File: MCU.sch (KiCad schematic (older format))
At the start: 5 parts, among them J1 Conn_01x05, J2 Conn_01x09, U2 STM32F051K8Tx

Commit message: UPDATED SWITCH WIRING
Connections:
- net labels added: MCU_IMON
- net labels removed: MCU_ISENSE, SMBUS_INT
- wire segments 51 -> 50
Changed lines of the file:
@@
 	5250 2800 5775 2800
 Text HLabel 5775 2800 2    50   Input ~ 0
-MCU_ISENSE
+MCU_IMON
 Wire Wire Line
 	5250 2900 5775 2900
@@
 SMBUS_SMBA
 Wire Wire Line
-	4150 4000 3250 4000
-Text HLabel 3250 4000 0    50   Input ~ 0
-SMBUS_INT
-Wire Wire Line
 	5775 3600 5250 3600

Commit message: replaced stm32F051 with stm32F072
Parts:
- removed J2: Conn_01x09, symbol Connector_Generic:Conn_01x09
- removed U2: STM32F051K8Tx, Package_QFP:LQFP-32_7x7mm_P0.8mm, symbol MCU_ST_STM32F0:STM32F051K8Tx
- added C1, C2, C3, C4, C5, C6: 100nF, Capacitor_SMD:C_0805_2012Metric_Pad1.15x1.40mm_HandSolder, symbol Device:C
- added J2: Conn_01x14, symbol Connector_Generic:Conn_01x14
- added L1: BEAD, Inductor_SMD:L_0805_2012Metric_Pad1.15x1.40mm_HandSolder, symbol Device:L_Small
- added R4: 10K, Resistor_SMD:R_0805_2012Metric_Pad1.15x1.40mm_HandSolder, symbol Device:R
- added U2: STM32F072RBTx, Package_QFP:LQFP-64_10x10mm_P0.5mm, symbol MCU_ST_STM32F0:STM32F072RBTx
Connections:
- net labels added: AVDD, TFT_MISO, T_CLK, T_CS, T_DIN, T_IRQ, T_OUT
- wire segments 50 -> 101
- no-connect marks 10 -> 30
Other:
- note added: "ICP SOCKET"
- note added: "TOUCHSCREEN TFT LCD"
- note removed: "TFT_MISO"
- moved on the sheet: J1, R1, R2

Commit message: layout draft
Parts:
- J1: footprint (none) -> Connector_PinHeader_2.54mm:PinHeader_1x05_P2.54mm_Vertical
- J2: footprint (none) -> Connector_PinHeader_2.54mm:PinHeader_1x14_P2.54mm_Vertical
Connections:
- net MCU_SW: now reaches U2.16 (PA2)
- no-connect marks 30 -> 29
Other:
- moved on the sheet: C1, L1, R1, R2, R4, U2

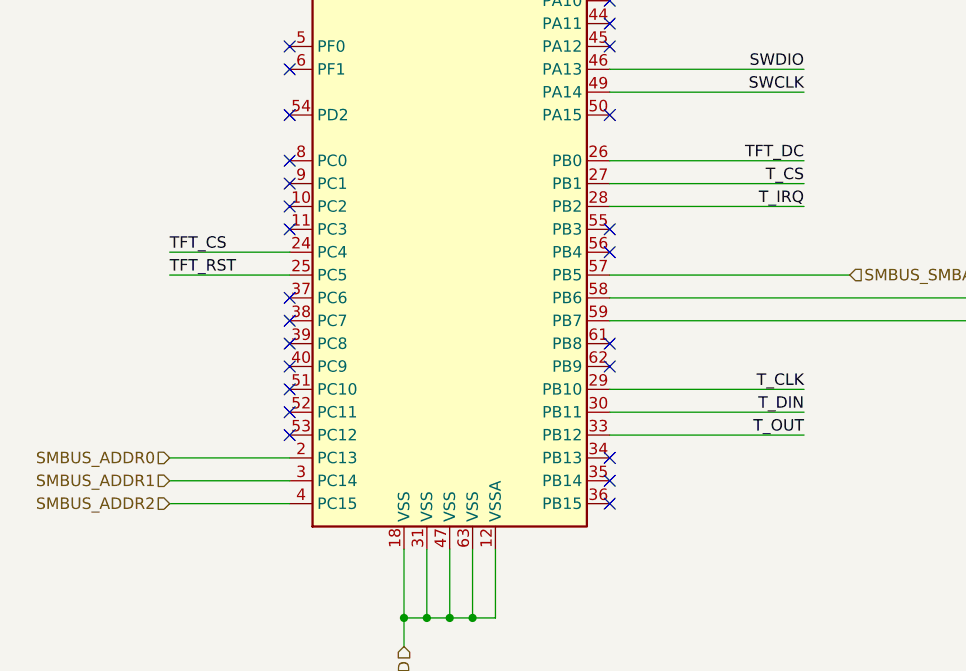
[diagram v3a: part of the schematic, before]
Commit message: moved SPI2 traces on MCU
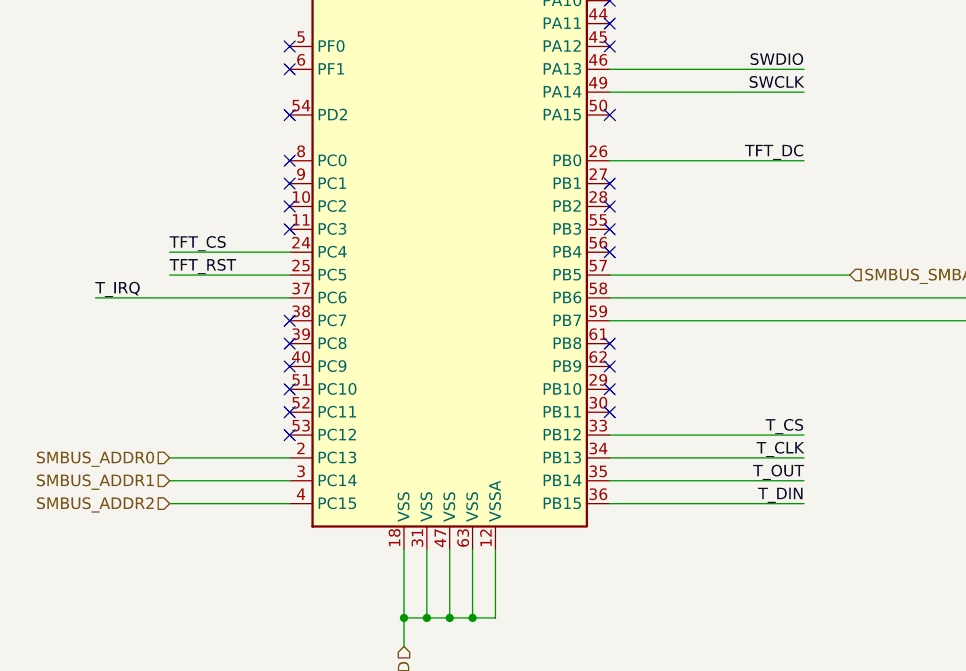
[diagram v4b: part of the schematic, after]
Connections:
- net T_CLK: now also U2.34 (PB13); no longer U2.29 (PB10)
- net T_CS: now also U2.33 (PB12); no longer U2.27 (PB1)
- net T_DIN: now also U2.36 (PB15); no longer U2.30 (PB11)
- net T_IRQ: now also U2.37 (PC6); no longer U2.28 (PB2)
- net T_OUT: now also U2.35 (PB14); no longer U2.33 (PB12)
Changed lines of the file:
@@
 TFT_MISO
 Wire Wire Line
-	4050 5350 4900 5350
-Wire Wire Line
-	4050 4450 4900 4450
-Wire Wire Line
-	4050 5450 4900 5450
+	4050 5650 4900 5650
 Wire Wire Line
 	4050 5550 4900 5550
 Wire Wire Line
-	4050 4550 4900 4550
-Text Label 4900 5350 2    50   ~ 0
+	4050 5850 4900 5850
+Wire Wire Line
+	4050 5750 4900 5750
+Wire Wire Line
+	2650 4950 1800 4950
+Text Label 4900 5650 2    50   ~ 0
 T_CLK
-Text Label 4900 4450 2    50   ~ 0
+Text Label 4900 5550 2    50   ~ 0
 T_CS
-Text Label 4900 5450 2    50   ~ 0
+Text Label 4900 5850 2    50   ~ 0
 T_DIN
-Text Label 4900 5550 2    50   ~ 0
+Text Label 4900 5750 2    50   ~ 0
 T_OUT
-Text Label 4900 4550 2    50   ~ 0
+Text Label 1800 4950 0    50   ~ 0
 T_IRQ
 NoConn ~ 4050 2950
@@
 NoConn ~ 4050 5150
 NoConn ~ 4050 5250
-NoConn ~ 4050 5650
-NoConn ~ 4050 5750
-NoConn ~ 4050 5850
 NoConn ~ 2650 5450
 NoConn ~ 2650 5350
@@
 NoConn ~ 2650 5150
 NoConn ~ 2650 5050
-NoConn ~ 2650 4950
+NoConn ~ 4050 4550
 NoConn ~ 2650 4650
 NoConn ~ 2650 4550
@@
 MCU_SW
 NoConn ~ 2650 5550
+NoConn ~ 4050 5350
+NoConn ~ 4050 5450
+NoConn ~ 4050 4450
 $EndSCHEMATC

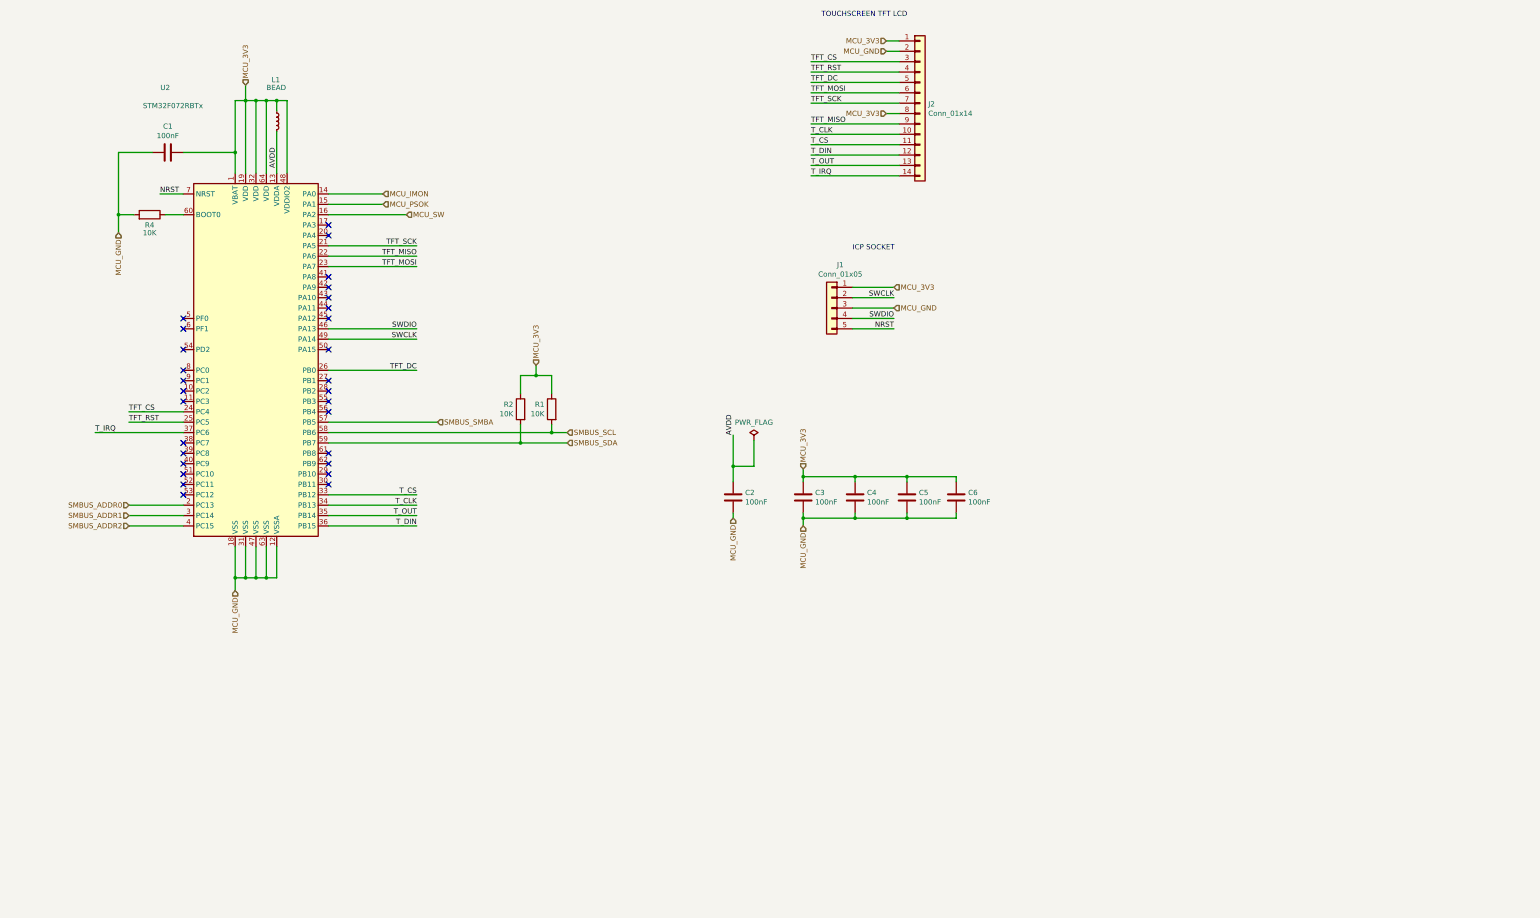
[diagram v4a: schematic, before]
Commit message: Added TFT Delayed Reset sub circuit
changed NCS1S1203SC to NCS1S1205SC
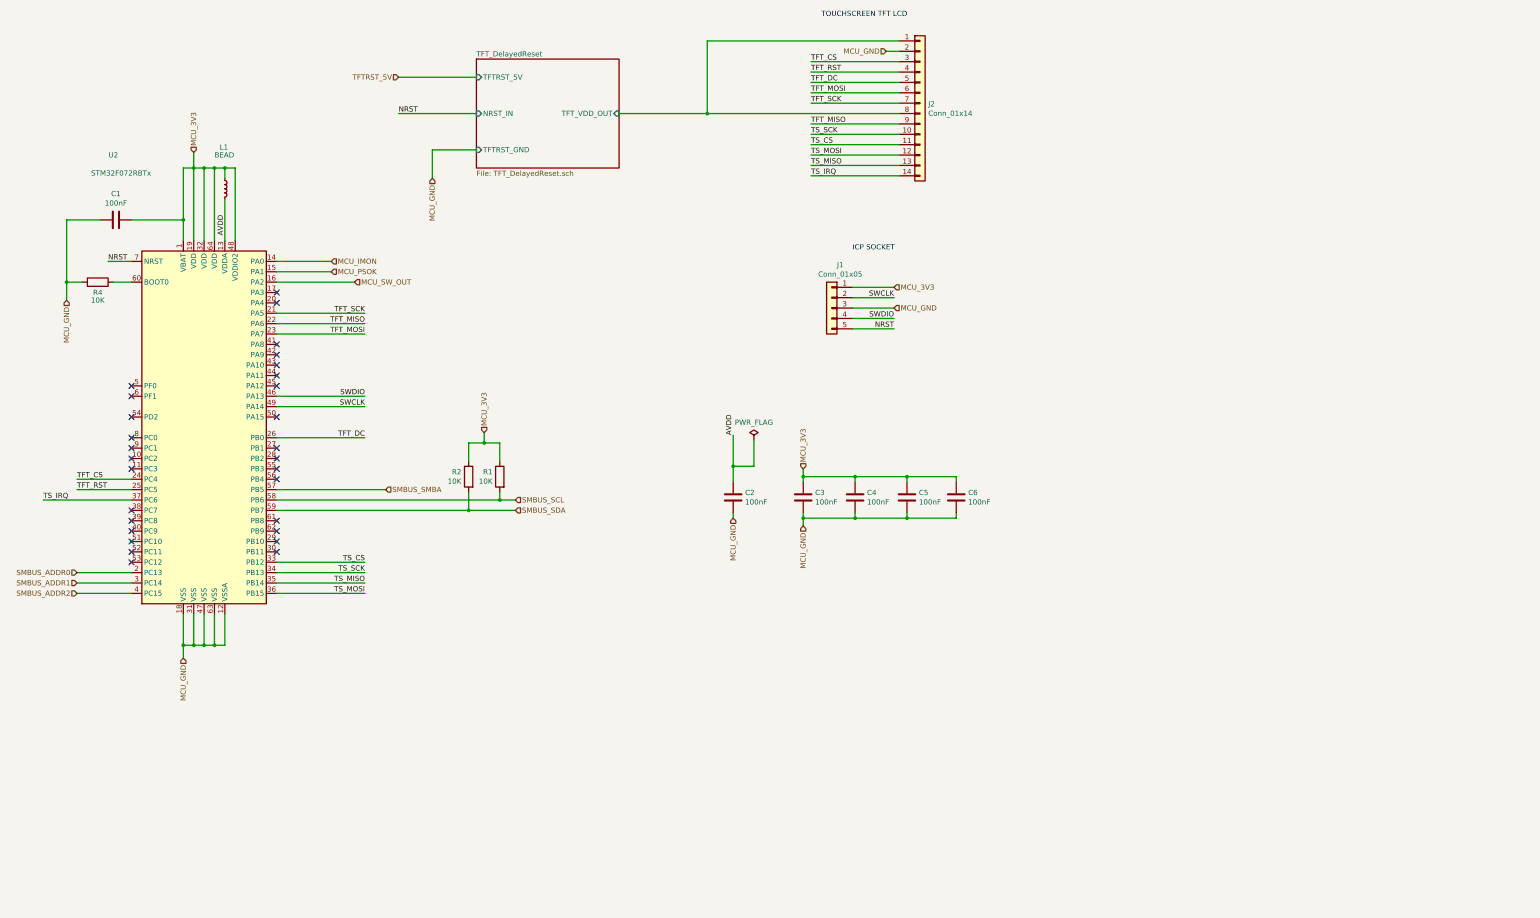
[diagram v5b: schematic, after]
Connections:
- net MCU_3V3: no longer J2.1 (Pin_1), J2.8 (Pin_8)
- net MCU_SW renamed MCU_SW_OUT
- net T_CLK renamed TS_SCK
- net T_CS renamed TS_CS
- net T_DIN renamed TS_MOSI
- net T_IRQ renamed TS_IRQ
- net T_OUT renamed TS_MISO
- new net TFT_DelayedReset/TFT_VDD_OUT: J2.1 (Pin_1), J2.8 (Pin_8)
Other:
- moved on the sheet: C1, L1, R1, R2, R4, U2

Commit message: updated hw
- added SMBUS address HW 
- Changed Isolated DC Module to TI SimpleSwitcher IC
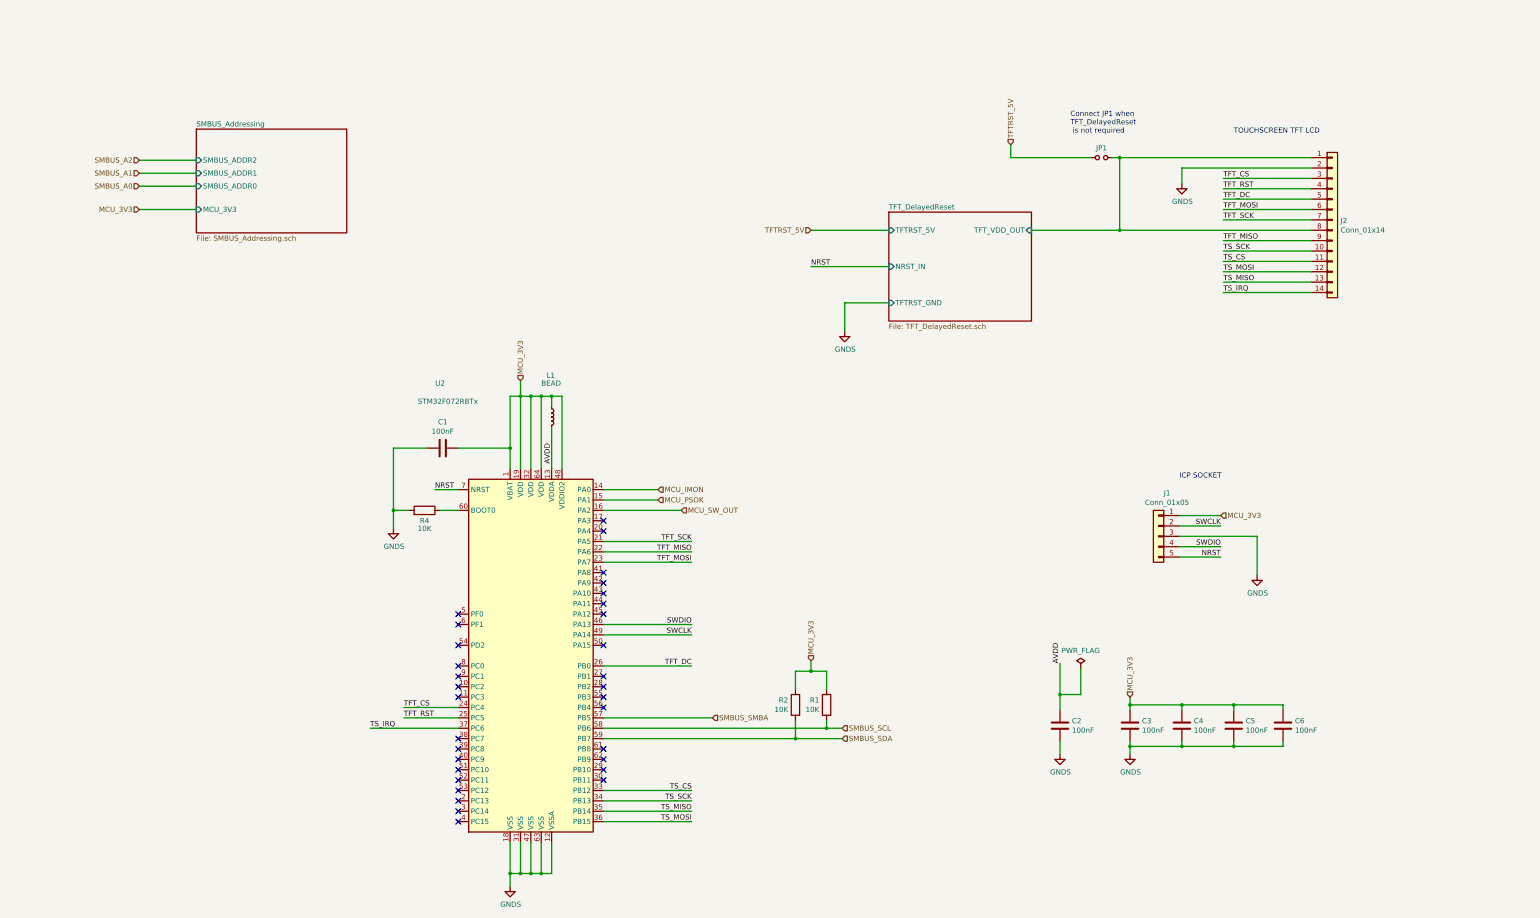
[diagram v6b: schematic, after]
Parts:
- added JP1: Jumper_NO_Small, Jumper:SolderJumper-2_P1.3mm_Open_Pad1.0x1.5mm, symbol Device:Jumper_NO_Small
- J1: footprint Connector_PinHeader_2.54mm:PinHeader_1x05_P2.54mm_Vertical -> Connector_PinHeader_2.54mm:PinHeader_1x05_P2.54mm_Horizontal
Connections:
- net TFTRST_5V: now also JP1.1
- net TFT_DelayedReset/TFT_VDD_OUT: now also JP1.2
- net MCU_GND renamed GNDS
- net SMBUS_ADDR0: no longer names the net of U2.2 (PC13)
- net SMBUS_ADDR1: no longer names the net of U2.3 (PC14)
- net SMBUS_ADDR2: no longer names the net of U2.4 (PC15)
- no-connect marks 29 -> 32
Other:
- note added: "Connect JP1 when\nTFT_DelayedReset\n is not required\n"
- moved on the sheet: C1, C2, C3, C4, C5, C6, J1, J2, L1, R1, R2, R4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

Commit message: Completed RevA
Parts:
- added TP1, TP2, TP? (x2): TestPoint, TestPoint:TestPoint_Pad_1.0x1.0mm, symbol Connector:TestPoint
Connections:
- net GNDS: now also TP2.1
- net MCU_3V3: now also TP1.1
- net SWCLK: now also TP?.1
- net SWDIO: now also TP?.1
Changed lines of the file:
@@
 $EndComp
 Wire Wire Line
-	12250 5750 12650 5750
+	12250 5750 13275 5750
 Wire Wire Line
 	12250 6050 12650 6050
@@
 Text Notes 12775 2075 0    50   ~ 0
 TOUCHSCREEN TFT LCD
-Text Notes 12250 5400 0    50   ~ 0
+Text Notes 11375 5975 0    50   ~ 0
 ICP SOCKET
 Wire Wire Line
@@
 NoConn ~ 6700 7300
 $Sheet
-S 9450 2825 1375 1050
+S 9450 2825 1375 700
 U 5F1755C4
 F0 "TFT_DelayedReset" 50
 F1 "TFT_DelayedReset.sch" 50
-F2 "TFTRST_GND" I L 9450 3700 50
 F3 "TFTRST_5V" I L 9450 3000 50
 F4 "TFT_VDD_OUT" I R 10825 3000 50
@@
 Wire Wire Line
 	11675 3000 13525 3000
-Wire Wire Line
-	9450 3700 9025 3700
-Wire Wire Line
-	9025 3700 9025 3975
 Text HLabel 11775 7500 1    50   Input ~ 0
 MCU_3V3
 Text HLabel 8700 7150 1    50   Input ~ 0
 MCU_3V3
-Text HLabel 12650 5750 2    50   Input ~ 0
+Text HLabel 13400 5750 2    50   Input ~ 0
 MCU_3V3
 Wire Wire Line
@@
 $EndComp
 Wire Wire Line
-	13000 5950 13000 6325
-Wire Wire Line
-	12250 5950 13000 5950
+	13825 5950 13825 6325
+Wire Wire Line
+	12250 5950 13825 5950
 $Comp
 L power:GNDS #PWR010
 U 1 1 5F506D40
-P 13000 6325
-F 0 "#PWR010" H 13000 6075 50  0001 C CNN
-F 1 "GNDS" H 13005 6152 50  0000 C CNN
-F 2 "" H 13000 6325 50  0001 C CNN
-F 3 "" H 13000 6325 50  0001 C CNN
-	1    13000 6325
+P 13825 6325
+F 0 "#PWR010" H 13825 6075 50  0001 C CNN
+F 1 "GNDS" H 13830 6152 50  0000 C CNN
+F 2 "" H 13825 6325 50  0001 C CNN
+F 3 "" H 13825 6325 50  0001 C CNN
+	1    13825 6325
 	1    0    0    -1
 $EndComp
@@
 Wire Wire Line
 	12275 2400 13525 2400
-$Comp
-L power:GNDS #PWR0103
-U 1 1 5F5B050D
-P 9025 3975
-F 0 "#PWR0103" H 9025 3725 50  0001 C CNN
-F 1 "GNDS" H 9030 3802 50  0000 C CNN
-F 2 "" H 9025 3975 50  0001 C CNN
-F 3 "" H 9025 3975 50  0001 C CNN
-	1    9025 3975
-	1    0    0    -1
-$EndComp
 Text Notes 11200 2075 0    50   ~ 0
 Connect JP1 when\nTFT_DelayedReset\n is not required\n
+$Comp
+L Connector:TestPoint TP1
+U 1 1 5F16AD63
+P 13275 5500
+F 0 "TP1" H 13333 5618 50  0000 L CNN
+F 1 "TestPoint" H 13333 5527 50  0000 L CNN
+F 2 "TestPoint:TestPoint_Pad_1.0x1.0mm" H 13475 5500 50  0001 C CNN
+F 3 "~" H 13475 5500 50  0001 C CNN
+	1    13275 5500
+	1    0    0    -1
+$EndComp
+Wire Wire Line
+	13275 5500 13275 5750
+Connection ~ 13275 5750
+Wire Wire Line
+	13275 5750 13400 5750
+$Comp
+L Connector:TestPoint TP2
+U 1 1 5F170479
+P 14025 5950
+F 0 "TP2" V 13950 6025 50  0000 L CNN
+F 1 "TestPoint" V 14125 6000 50  0000 L CNN
+F 2 "TestPoint:TestPoint_Pad_1.0x1.0mm" H 14225 5950 50  0001 C CNN
+F 3 "~" H 14225 5950 50  0001 C CNN
+	1    14025 5950
+	0    1    1    0
+$EndComp
+Wire Wire Line
+	14025 5950 13825 5950
+Connection ~ 13825 5950
+$Comp
+L Connector:TestPoint TP?
+U 1 1 5F271D97
+P 14650 5100
+AR Path="/5F02F4E9/5F271D97" Ref="TP?"  Part="1"
+AR Path="/5EFF0F4B/5F271D97" Ref="TP?"  Part="1"
+F 0 "TP?" H 14708 5218 50  0000 L CNN
+F 1 "TestPoint" H 14708 5127 50  0000 L CNN
+F 2 "TestPoint:TestPoint_Pad_1.0x1.0mm" H 14850 5100 50  0001 C CNN
+F 3 "~" H 14850 5100 50  0001 C CNN
+	1    14650 5100
+	1    0    0    -1
+$EndComp
+$Comp
+L Connector:TestPoint TP?
+U 1 1 5F275A4B
+P 15150 5100
+AR Path="/5F02F4E9/5F275A4B" Ref="TP?"  Part="1"
+AR Path="/5EFF0F4B/5F275A4B" Ref="TP?"  Part="1"
+F 0 "TP?" H 15208 5218 50  0000 L CNN
+F 1 "TestPoint" H 15208 5127 50  0000 L CNN
+F 2 "TestPoint:TestPoint_Pad_1.0x1.0mm" H 15350 5100 50  0001 C CNN
+F 3 "~" H 15350 5100 50  0001 C CNN
+	1    15150 5100
+	1    0    0    -1
+$EndComp
+Text Label 14650 5425 1    50   ~ 0
+SWCLK
+Wire Wire Line
+	14650 5100 14650 5425
+Text Label 15150 5425 1    50   ~ 0
+SWDIO
+Wire Wire Line
+	15150 5100 15150 5425
 $EndSCHEMATC

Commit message: save
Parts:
- J2: footprint Connector_PinHeader_2.54mm:PinHeader_1x14_P2.54mm_Vertical -> ILI9341_TFTLCD:ILI9341_ResitiveTouch_TFTLCD_2.8inch_85mm_50mm
- gave numbers to parts that had none: 2
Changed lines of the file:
@@
 F 0 "J2" H 13805 2892 50  0000 L CNN
 F 1 "Conn_01x14" H 13805 2801 50  0000 L CNN
-F 2 "Connector_PinHeader_2.54mm:PinHeader_1x14_P2.54mm_Vertical" H 13725 2900 50  0001 C CNN
+F 2 "ILI9341_TFTLCD:ILI9341_ResitiveTouch_TFTLCD_2.8inch_85mm_50mm" H 13725 2900 50  0001 C CNN
 F 3 "~" H 13725 2900 50  0001 C CNN
 	1    13725 2900
@@
 Connection ~ 13825 5950
 $Comp
-L Connector:TestPoint TP?
+L Connector:TestPoint TP22
 U 1 1 5F271D97
 P 14650 5100
-AR Path="/5F02F4E9/5F271D97" Ref="TP?"  Part="1"
+AR Path="/5F02F4E9/5F271D97" Ref="TP22"  Part="1"
 AR Path="/5EFF0F4B/5F271D97" Ref="TP?"  Part="1"
-F 0 "TP?" H 14708 5218 50  0000 L CNN
+F 0 "TP22" H 14708 5218 50  0000 L CNN
 F 1 "TestPoint" H 14708 5127 50  0000 L CNN
 F 2 "TestPoint:TestPoint_Pad_1.0x1.0mm" H 14850 5100 50  0001 C CNN
@@
 $EndComp
 $Comp
-L Connector:TestPoint TP?
+L Connector:TestPoint TP23
 U 1 1 5F275A4B
 P 15150 5100
-AR Path="/5F02F4E9/5F275A4B" Ref="TP?"  Part="1"
+AR Path="/5F02F4E9/5F275A4B" Ref="TP23"  Part="1"
 AR Path="/5EFF0F4B/5F275A4B" Ref="TP?"  Part="1"
-F 0 "TP?" H 15208 5218 50  0000 L CNN
+F 0 "TP23" H 15208 5218 50  0000 L CNN
 F 1 "TestPoint" H 15208 5127 50  0000 L CNN
 F 2 "TestPoint:TestPoint_Pad_1.0x1.0mm" H 15350 5100 50  0001 C CNN
